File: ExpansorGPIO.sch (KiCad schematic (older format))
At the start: 15 parts, among them P4 CONN_01X03, P5 CONN_01X03, P6 CONN_01X03, P7 CONN_01X03, U6 PCA9551

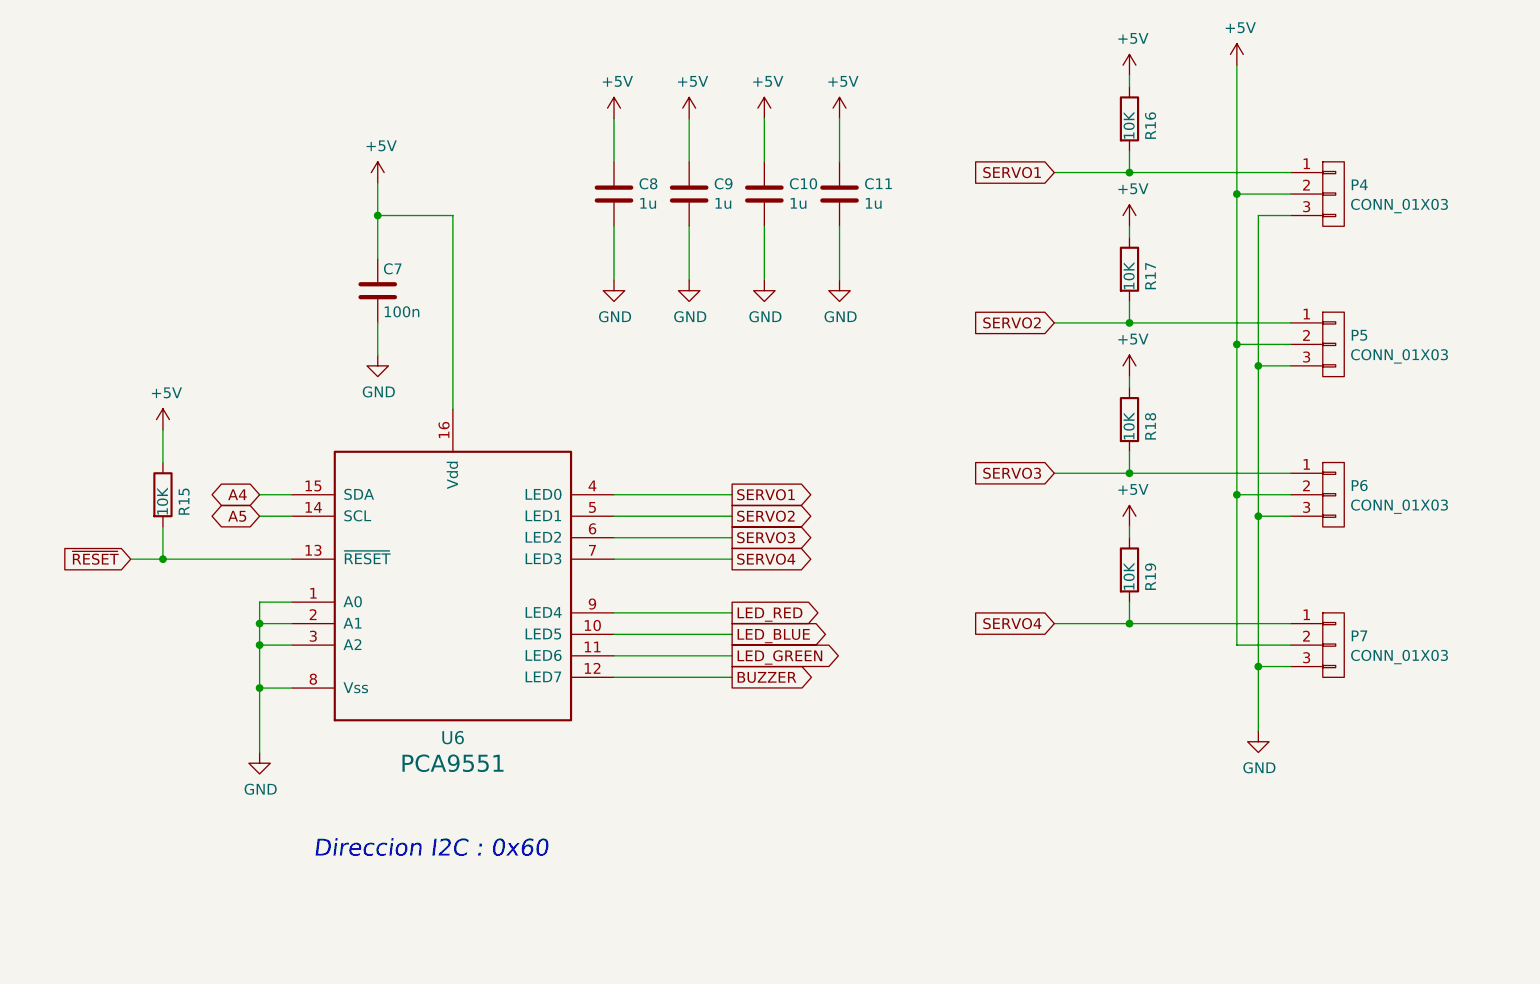
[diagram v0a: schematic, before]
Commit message: Se añade un expansor GPIO al esquema y se elminan registros y codificador
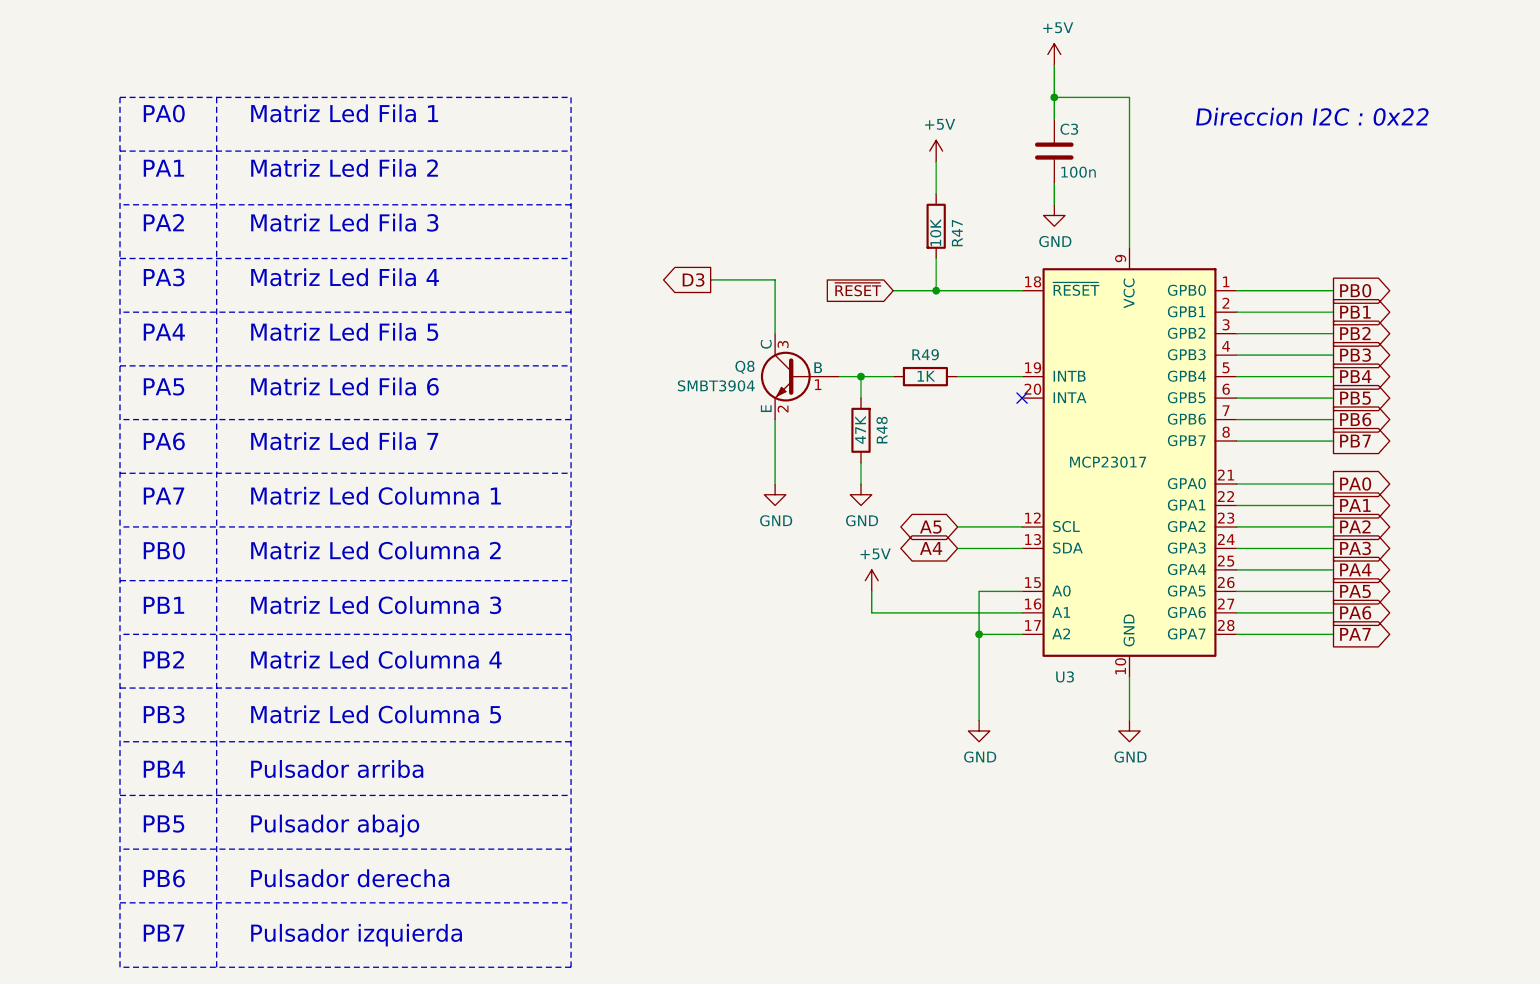
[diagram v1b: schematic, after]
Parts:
- removed C10, C11, C8, C9: 1u, Capacitors_SMD:C_0805, symbol C
- removed C7: 100n, Capacitors_SMD:C_0805, symbol C
- removed P4, P5, P6, P7: CONN_01X03, Pin_Headers:Pin_Header_Straight_1x03_Pitch2.54mm, symbol CONN_01X03
- removed R15, R16, R17, R18, R19: 10K, Resistencias:R_0805, symbol R
- removed U6: PCA9551, Housings_SSOP:TSSOP-16_4.4x5mm_Pitch0.65mm, symbol PCA9551
- added C3: 100n, Capacitors_SMD:C_0805, symbol C
- added Q8: SMBT3904, TO_SOT_Packages_SMD:SOT-23, symbol BC849
- added R47: 10K, Resistencias:R_0805, symbol R
- added R48: 47K, Resistencias:R_0805, symbol R
- added R49: 1K, Resistencias:R_0805, symbol R
- added U3: MCP23017, Housings_SSOP:TSSOP-28_4.4x9.7mm_Pitch0.65mm, symbol MCP23017
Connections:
- net +5V: now also C3.1, R47.1, U3.16 (A1), U3.9 (VCC)
- net A4: now also U3.13 (SDA)
- net A5: now also U3.12 (SCL)
- net GND: now also C3.2, Q8.2 (E), R48.1, U3.10 (GND), U3.15 (A0), U3.17 (A2)
- net ~RESET: now also R47.2, U3.18 (~RESET)
- new net: R49.1, U3.19 (INTB)
- new net: Q8.1 (B), R48.2, R49.2
- new net D3: Q8.3 (C)
- new net PA0: U3.21 (GPA0)
- new net PA1: U3.22 (GPA1)
- new net PA2: U3.23 (GPA2)
- new net PA3: U3.24 (GPA3)
- new net PA4: U3.25 (GPA4)
- new net PA5: U3.26 (GPA5)
- new net PA6: U3.27 (GPA6)
- new net PA7: U3.28 (GPA7)
- new net PB0: U3.1 (GPB0)
- new net PB1: U3.2 (GPB1)
- new net PB2: U3.3 (GPB2)
- new net PB3: U3.4 (GPB3)
- new net PB4: U3.5 (GPB4)
- new net PB5: U3.6 (GPB5)
- new net PB6: U3.7 (GPB6)
- new net PB7: U3.8 (GPB7)
- no-connect marks 0 -> 1
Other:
- note added: "Direccion I2C : 0x22"
- note added: "Matriz Led Fila 1\n\nMatriz Led Fila 2\n\nMatriz Led Fila 3\n\nMatriz Led Fila 4\n\nMatriz Led Fila 5\n\nMatriz Led Fila 6\n\nMatriz Led Fila 7\n\nMatriz Led Columna 1\n\nMatriz Led Columna 2\n\nMatriz Led Columna 3\n\nMatriz Led Columna 4\n\nMatriz Led Columna 5\n\nPulsador arriba\n\nPulsador abajo\n\nPulsador derecha\n\nPulsador izquierda"
- note added: "PA0\n\nPA1\n\nPA2\n\nPA3\n\nPA4\n\nPA5\n\nPA6\n\nPA7\n\nPB0\n\nPB1\n\nPB2\n\nPB3\n\nPB4\n\nPB5\n\nPB6\n\nPB7"
- note removed: "Direccion I2C : 0x60"

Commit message: Revisado V0.4. Actualizados gerber y esquemas
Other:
- note added: "Matriz Led Fila 1\n\nMatriz Led Fila 2\n\nMatriz Led Fila 3\n\nMatriz Led Fila 4\n\nMatriz Led Fila 5\n\nMatriz Led Fila 6\n\nMatriz Led Fila 7\n\nMatriz Led Columna 1\n\nPulsador abajo\n\nPulsador izquierda\n\nPulsador derecha\n\nPusador arriba\n\nMatriz Led Columna 2\n\nMatriz Led Columna 3\n\nMatriz Led Columna 4\n\nMatriz Led Columna 5\n"
- note removed: "Matriz Led Fila 1\n\nMatriz Led Fila 2\n\nMatriz Led Fila 3\n\nMatriz Led Fila 4\n\nMatriz Led Fila 5\n\nMatriz Led Fila 6\n\nMatriz Led Fila 7\n\nMatriz Led Columna 1\n\nMatriz Led Columna 2\n\nMatriz Led Columna 3\n\nMatriz Led Columna 4\n\nMatriz Led Columna 5\n\nPulsador arriba\n\nPulsador abajo\n\nPulsador derecha\n\nPulsador izquierda"
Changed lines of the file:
@@
 Sheet 4 17
 Title "Expansor de GPIO's"
-Date "2017-01-19"
+Date "2017-01-25"
 Rev "V.0.4"
 Comp "NanoPlayBoard"
@@
 PA0\n\nPA1\n\nPA2\n\nPA3\n\nPA4\n\nPA5\n\nPA6\n\nPA7\n\nPB0\n\nPB1\n\nPB2\n\nPB3\n\nPB4\n\nPB5\n\nPB6\n\nPB7
 Text Notes 1500 4850 0    79   ~ 0
-Matriz Led Fila 1\n\nMatriz Led Fila 2\n\nMatriz Led Fila 3\n\nMatriz Led Fila 4\n\nMatriz Led Fila 5\n\nMatriz Led Fila 6\n\nMatriz Led Fila 7\n\nMatriz Led Columna 1\n\nMatriz Led Columna 2\n\nMatriz Led Columna 3\n\nMatriz Led Columna 4\n\nMatriz Led Columna 5\n\nPulsador arriba\n\nPulsador abajo\n\nPulsador derecha\n\nPulsador izquierda
+Matriz Led Fila 1\n\nMatriz Led Fila 2\n\nMatriz Led Fila 3\n\nMatriz Led Fila 4\n\nMatriz Led Fila 5\n\nMatriz Led Fila 6\n\nMatriz Led Fila 7\n\nMatriz Led Columna 1\n\nPulsador abajo\n\nPulsador izquierda\n\nPulsador derecha\n\nPusador arriba\n\nMatriz Led Columna 2\n\nMatriz Led Columna 3\n\nMatriz Led Columna 4\n\nMatriz Led Columna 5\n
 Wire Notes Line
 	900  900  3000 900

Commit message: corregidos valores en esquema y simbolos corruptos
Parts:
- U3: footprint Housings_SSOP:TSSOP-28_4.4x9.7mm_Pitch0.65mm -> Housings_SSOP:SSOP-28_5.3x10.2mm_Pitch0.65mm
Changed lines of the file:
@@
 EESchema Schematic File Version 2
+LIBS:Nano_PB-rescue
 LIBS:Interfaces
-LIBS:Nano_PB-rescue
 LIBS:Sensores
 LIBS:power
@@
 LIBS:matriz_led
 LIBS:Pasivos
+LIBS:Reles
 LIBS:Nano_PB-cache
 EELAYER 26 0
@@
 F 0 "U3" H 5900 1600 50  0000 C CNN
 F 1 "MCP23017" H 5700 2600 50  0000 C CNN
-F 2 "Housings_SSOP:TSSOP-28_4.4x9.7mm_Pitch0.65mm" H 5650 1650 50  0001 L CNN
+F 2 "Housings_SSOP:SSOP-28_5.3x10.2mm_Pitch0.65mm" H 5650 1650 50  0001 L CNN
 F 3 "" H 5850 3600 50  0001 C CNN
 	1    5600 2600
@@
 $Bitmap
 Pos 7500 4400
-Scale 0,350000
+Scale 0,000000
 Data
 89 50 4E 47 0D 0A 1A 0A 00 00 00 0D 49 48 44 52 00 00 01 D5 00 00 01 ED 08 06 00 00 00 4F 90 E4
